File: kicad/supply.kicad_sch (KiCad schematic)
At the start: 60 parts, among them U2 TLV62565DBVR, U3 TLV62565DBVR, U4 TLV62565DBVR

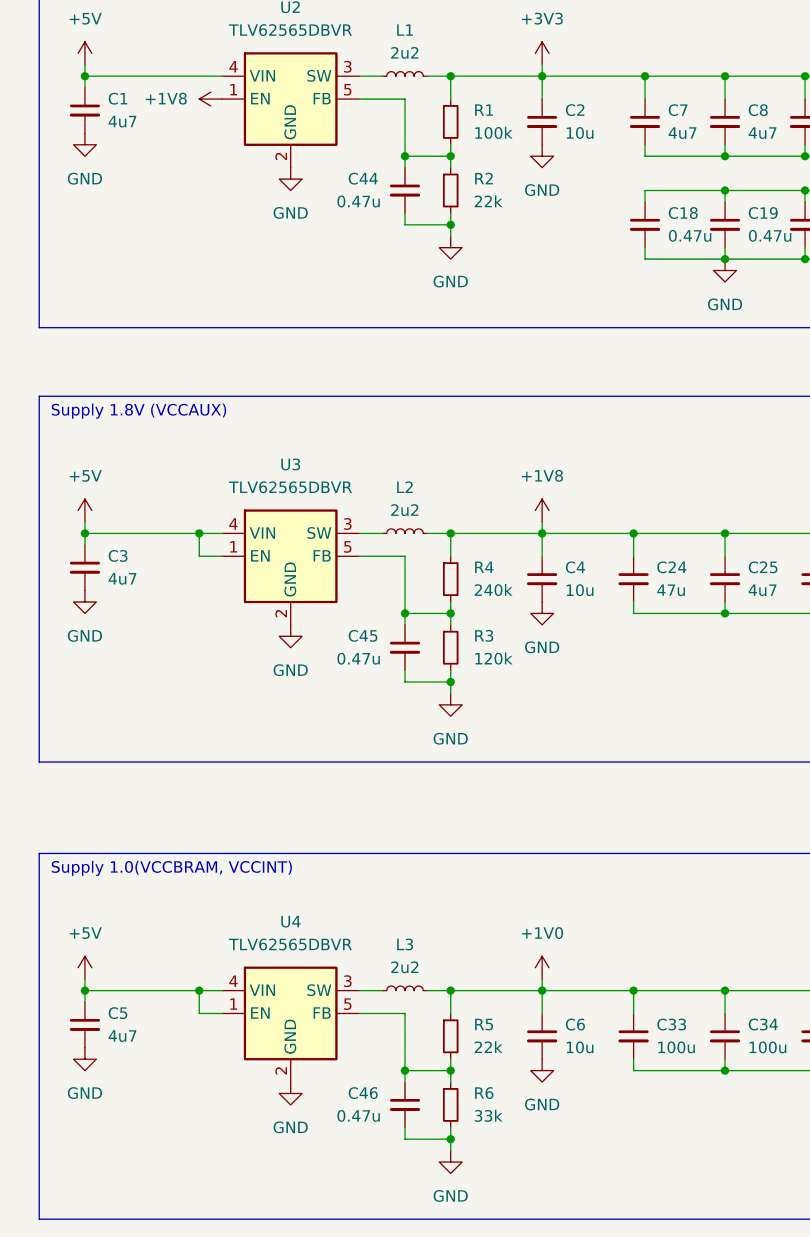
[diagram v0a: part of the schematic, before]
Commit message: Supply fb resistor marked as Not Populated
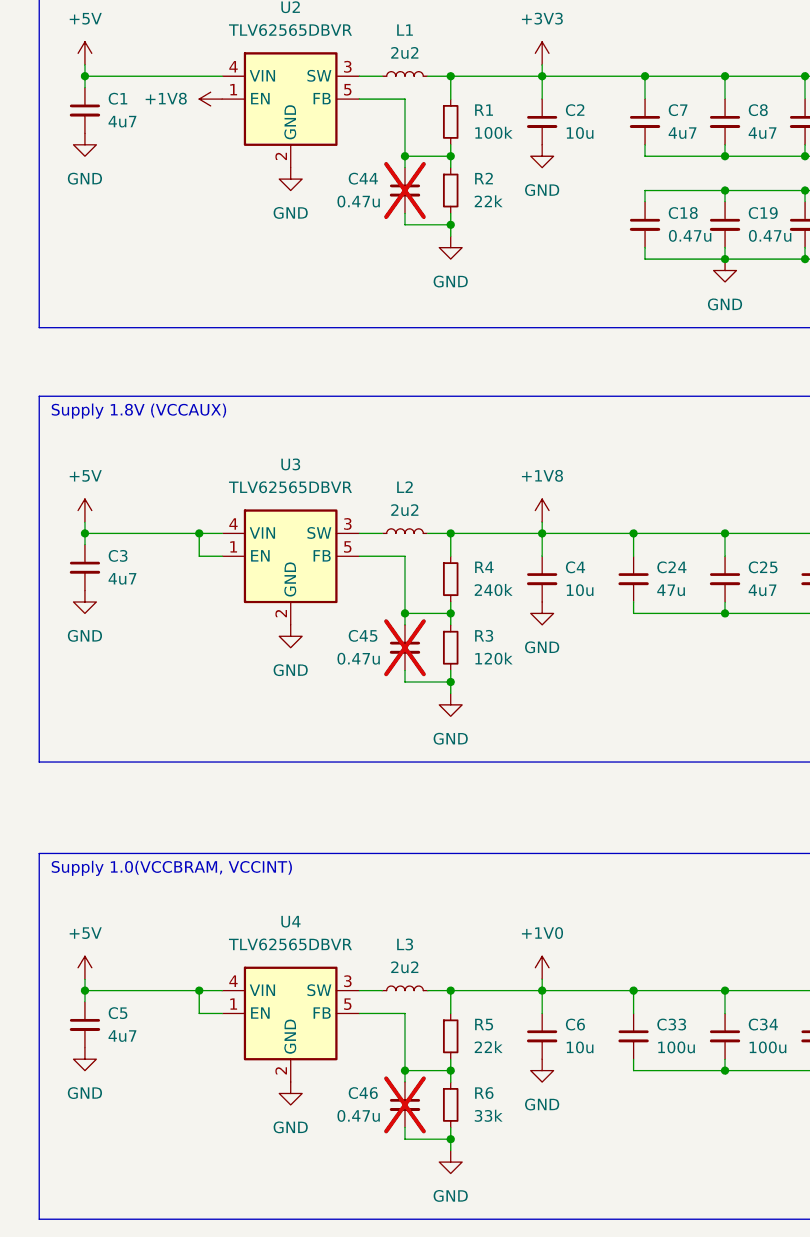
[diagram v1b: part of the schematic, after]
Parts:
- C44, C45, C46: now not fitted
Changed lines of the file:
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@@
   )
   (symbol (lib_id "Device:C_Small") (at 168.91 185.42 0) (unit 1)
-    (in_bom yes) (on_board yes) (dnp no)
+    (in_bom yes) (on_board yes) (dnp yes)
     (property "Reference" "C46" (at 162.56 184.15 0)
       (effects (font (size 1.27 1.27)) (justify left))
@@
   )
   (symbol (lib_id "Device:C_Small") (at 168.91 83.82 0) (unit 1)
-    (in_bom yes) (on_board yes) (dnp no)
+    (in_bom yes) (on_board yes) (dnp yes)
     (property "Reference" "C44" (at 162.56 82.55 0)
       (effects (font (size 1.27 1.27)) (justify left))
@@
   )
   (symbol (lib_id "Device:C_Small") (at 168.91 134.62 0) (unit 1)
-    (in_bom yes) (on_board yes) (dnp no)
+    (in_bom yes) (on_board yes) (dnp yes)
     (property "Reference" "C45" (at 162.56 133.35 0)
       (effects (font (size 1.27 1.27)) (justify left))
